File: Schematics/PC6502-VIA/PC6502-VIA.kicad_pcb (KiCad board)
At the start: 4 copper layers, 100 x 100 mm, 38 parts, among them J1 BUS, J2 Conn_02x06_Odd_Even, J3 Conn_02x06_Odd_Even, J4 Conn_02x04_Odd_Even, J5 Conn_02x04_Odd_Even, J6 Conn_02x06_Odd_Even, J7 Conn_02x06_Odd_Even, J8 Conn_02x05_Odd_Even, U1 W65C22NxP, U2 W65C22NxP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

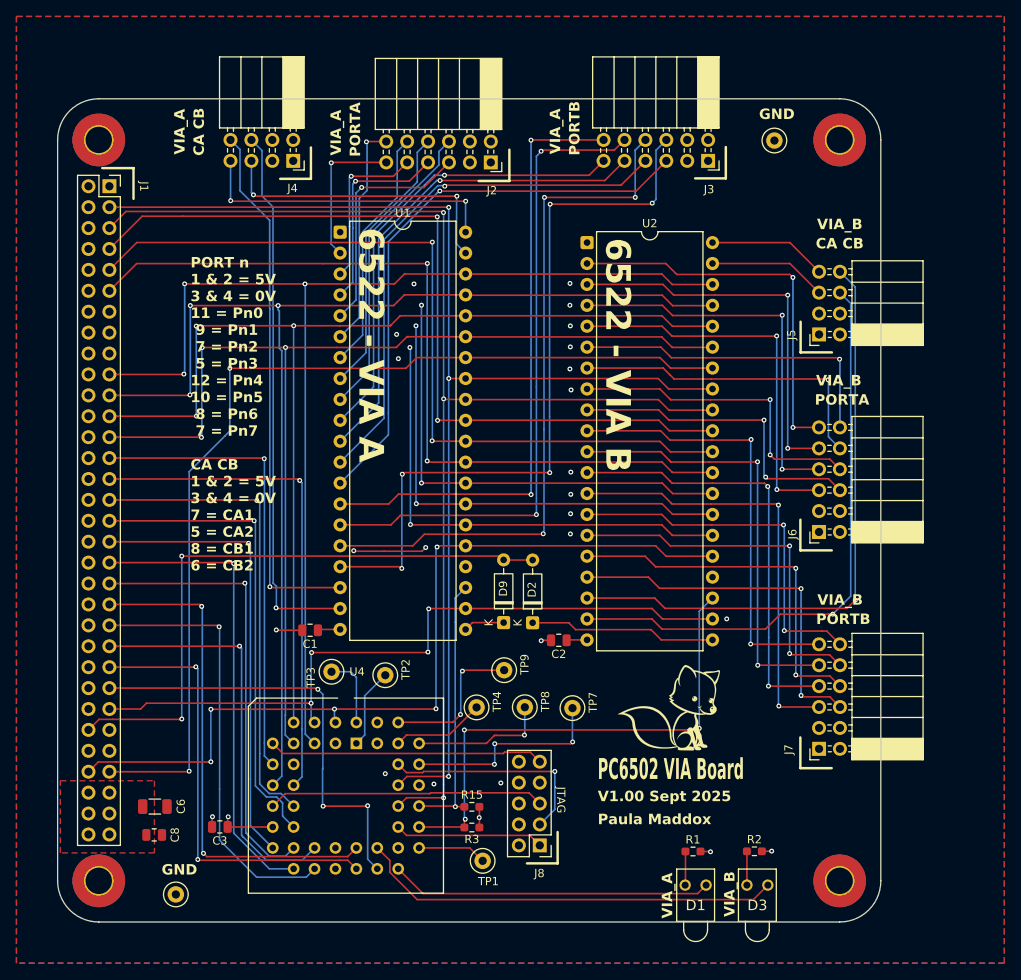
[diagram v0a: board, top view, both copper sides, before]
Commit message: V1.1 CPU, VIA and POWER PCBs uploaded
A simpler CPU board (direct link to FT245R, 74161 removed and some tidying of tracks). Fixed a couple of floating inputs to RAM/ROM
VIA is much simpler, having just the one VIA chip.
POWER board has USB-PD and a 24VDC input for higher power stuff in the future.
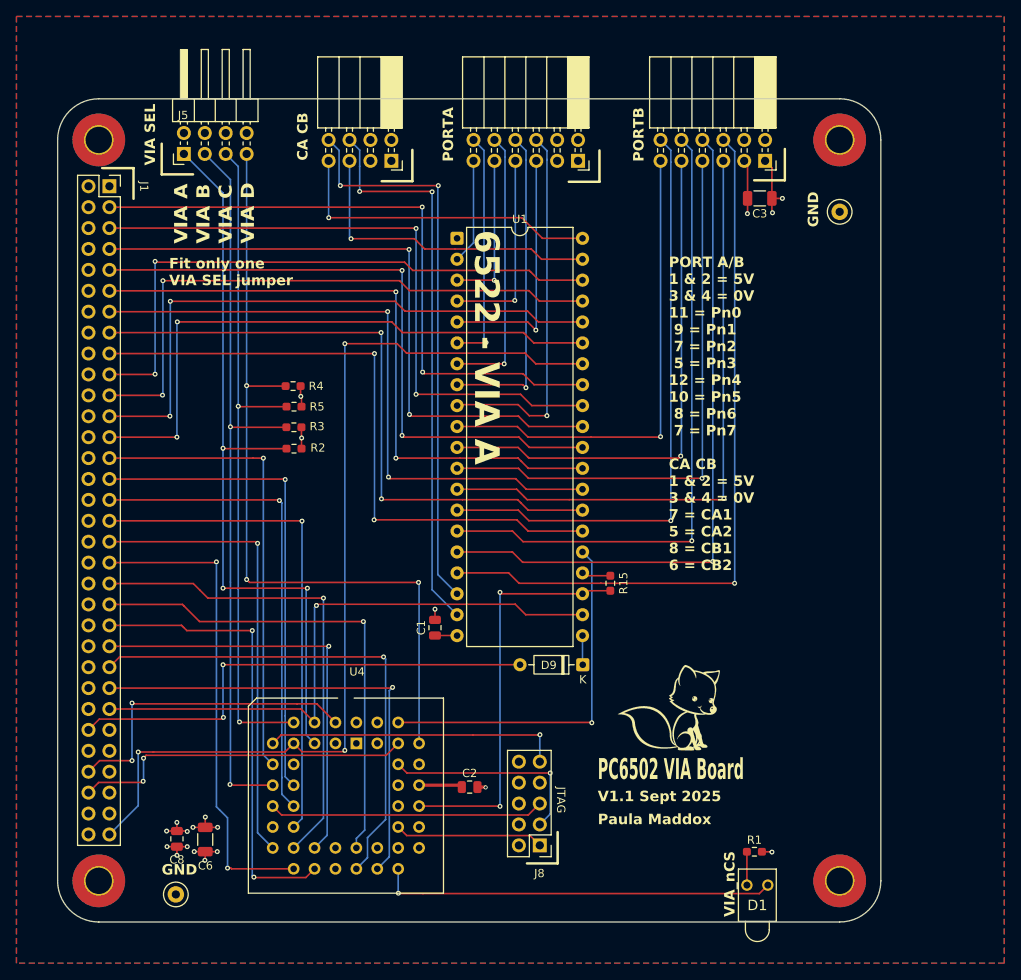
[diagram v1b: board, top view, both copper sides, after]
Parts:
- removed D2: 1N4148, Diode_THT:D_DO-35_SOD27_P7.62mm_Horizontal
- removed D3: LED, LTL-4221NHBP:LTL4221NHBP
- removed J6, J7: Conn_02x06_Odd_Even, Connector_PinSocket_2.54mm:PinSocket_2x06_P2.54mm_Horizontal
- removed TP1, TP2, TP3, TP4, TP7, TP8, TP9: TestPoint, TestPoint:TestPoint_Loop_D1.80mm_Drill1.0mm_Beaded
- removed U2: W65C22NxP, Package_DIP:DIP-40_W15.24mm
- added R4: 4K7, Resistor_SMD:R_0603_1608Metric_Pad0.98x0.95mm_HandSolder, F.Cu at (125.7, 79.9)
- added R5: 4K7, Resistor_SMD:R_0603_1608Metric_Pad0.98x0.95mm_HandSolder, F.Cu at (125.8, 82.4)
- C3: value 100nF -> 47uF; footprint Capacitor_SMD:C_0805_2012Metric -> Capacitor_SMD:C_1206_3216Metric
- J5: value Conn_02x04_Odd_Even -> VIA_SEL; footprint Connector_PinSocket_2.54mm:PinSocket_2x04_P2.54mm_Horizontal -> Connector_PinHeader_2.54mm:PinHeader_2x04_P2.54mm_Horizontal
- R2: value 470R -> 4K7
- moved C3 100.6 mm to (182.3, 57.1)
- moved J5 80.2 mm to (112.4, 51.7), turned to 90 degrees
- moved R2 74.3 mm to (125.8, 87.5), turned to 180 degrees
- moved R3 53.2 mm to (125.8, 84.9)
- moved R15 31.9 mm to (164.2, 103.8), turned to -90 degrees
- moved C2 20.9 mm to (147.1, 128.6), turned to 0 degrees
- moved C1 15.2 mm to (142.9, 109.2), turned to 90 degrees
- moved U1 14.2 mm to (145.6, 62.0)
- moved J4 11.9 mm to (137.6, 52.5)
- moved TP6 11.7 mm to (192.1, 58.7), turned to 90 degrees
- moved D9 10.9 mm to (160.8, 113.8), turned to 180 degrees
- moved J2 10.6 mm to (160.3, 52.5)
- moved D1 7.50 mm to (180.8, 140.5)
- moved R1 7.46 mm to (181.7, 136.5)
- moved C6 7.31 mm to (115.0, 135.0), turned to -90 degrees
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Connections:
- net nSLOW renamed nSLOW0
- J1 pad 12: GND -> +5V
- J1 pad 16: GND -> +5V
- J1 pad 20: GND -> +5V
- J1 pad 24: GND -> +5V
- J1 pad 28: GND -> +5V
- J1 pad 32: GND -> +5V
- J1 pad 36: GND -> +5V
- J1 pad 4: GND -> +5V
- J1 pad 40: GND -> +5V
- J1 pad 44: GND -> +5V
- J1 pad 48: GND -> +5V
- J1 pad 55: nBUSRQ -> nSLOW1
- J1 pad 57: nRES -> RDY
- J1 pad 58: CLK -> SYSCLK
- J1 pad 59: +5V -> nVP
- J1 pad 60: SPCLK -> CPU_CLK
- J1 pad 61: +5V -> nBUSRQ
- J1 pad 62: +5V -> unconnected-(J1-Pin_62-Pad62)
- J1 pad 63: +5V -> nRES
- J1 pad 64: +5V -> GND
- J1 pad 8: GND -> +5V
- J3 pad 1: unconnected-(J3-Pin_1-Pad1) -> +5V
- J4 pad 1: unconnected-(J4-Pin_1-Pad1) -> +5V
- J5 pad 1: +5V -> VIA_SEL0
- J5 pad 2: +5V -> GND
- J5 pad 3: GND -> VIA_SEL1
- J5 pad 5: /VB_CA2 -> VIA_SEL2
- J5 pad 6: /VB_CB2 -> GND
- J5 pad 7: /VB_CA1 -> VIA_SEL3
- J5 pad 8: /VB_CB1 -> GND
- R2 pad 1: Net-(D3-A) -> +5V
- R2 pad 2: +5V -> VIA_SEL0
- R3 pad 2: 6522B_CS -> VIA_SEL1
- U1 pad 25: CLK -> VIA_CLK
- U4 pad 1: Net-(U4-I/GCLR) -> unconnected-(U4-I/GCLR-Pad1)
- U4 pad 11: /A1 -> VIA_SEL1
- U4 pad 2: CLK -> SYSCLK
- U4 pad 27: Net-(D3-K) -> unconnected-(U4-I/O-Pad27)
- U4 pad 29: Net-(TP1-Pad1) -> unconnected-(U4-I/O-Pad29)
- U4 pad 31: 6522B_CS -> unconnected-(U4-I/O-Pad31)
- U4 pad 34: /D1 -> unconnected-(U4-I/O-Pad34)
- U4 pad 36: /D0 -> unconnected-(U4-I/O-Pad36)
- U4 pad 37: Net-(TP7-Pad1) -> unconnected-(U4-I/O-Pad37)
- U4 pad 39: Net-(TP8-Pad1) -> VIA_SEL3
- U4 pad 40: Net-(TP9-Pad1) -> VIA_CLK
- U4 pad 41: Net-(U4-I/O/GCLK3) -> CPU_CLK
- U4 pad 44: Net-(U4-I/OE1) -> unconnected-(U4-I/OE1-Pad44)
- U4 pad 5: /A0 -> VIA_SEL0
- U4 pad 6: /A2 -> VIA_SEL2
- U4 pad 8: /A3 -> nRES
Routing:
- net CLK: track 104.5 -> 0.00 mm, vias 5 -> 0
- net VIA_SEL3: track 0.00 -> 97.2 mm, vias 0 -> 3
- net VIA_SEL0: track 0.00 -> 92.0 mm, vias 0 -> 3
- net VIA_SEL1: track 0.00 -> 90.0 mm, vias 0 -> 2
- net VIA_SEL2: track 0.00 -> 82.2 mm, vias 0 -> 2
- net /VB_CB1: track 74.2 -> 0.00 mm, vias 1 -> 0
- net /D1: track 151.7 -> 78.2 mm, vias 3 -> 2
- net /A1: track 144.1 -> 72.4 mm, vias 3 -> 2
- net /VB_CB2: track 71.6 -> 0.00 mm, vias 1 -> 0
- net /D0: track 149.5 -> 78.1 mm, vias 3 -> 2
- net /A0: track 141.5 -> 72.1 mm, vias 3 -> 2
- net 6522B_CS: track 62.6 -> 0.00 mm, vias 3 -> 0
- net /A3: track 133.7 -> 72.5 mm, vias 3 -> 2
- net /A2: track 133.5 -> 72.4 mm, vias 3 -> 2
- net /VB_PB0: track 53.6 -> 0.00 mm, vias 2 -> 0
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- removed copper zone on F.Cu, net +5V
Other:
- board text added: "Fit only one VIA SEL jumper"
- board text added: "PORT A/B 1 & 2 = 5V 3 & 4 = 0V 11 = Pn0 9 = Pn1 7 = Pn2 5 = Pn3 12 = Pn4 10 = Pn5 8 = Pn6 7 = Pn7 CA CB 1 & 2 = 5V 3 & 4 = 0V 7 = CA1 5 = CA2 8 = CB1 6 = CB2"
- board text added: "V1.1 Sept 2025"
- board text added: "VIA A"
- board text added: "VIA B"
- board text added: "VIA C"
- board text added: "VIA D"
- board text added: "VIA SEL"
- board text added: "VIA_nCS"
- board text removed: "6522 - VIA B"
- board text removed: "PORT n 1 & 2 = 5V 3 & 4 = 0V 11 = Pn0 9 = Pn1 7 = Pn2 5 = Pn3 12 = Pn4 10 = Pn5 8 = Pn6 7 = Pn7 CA CB 1 & 2 = 5V 3 & 4 = 0V 7 = CA1 5 = CA2 8 = CB1 6 = CB2"
- board text removed: "V1.00 Sept 2025"
- board text removed: "VIA_A"
- board text removed: "VIA_B"

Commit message: Ordered Storage, FM/Speech, Dual SPI and APPLE II slot PCBs
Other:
- board text added: "PORT A/B 1 & 2 = 5V 3 & 4 = 0V 11 = Pn0 9 = Pn1 7 = Pn2 5 = Pn3 12 = Pn4 10 = Pn5 8 = Pn6 6 = Pn7 CA CB 1 & 2 = 5V 3 & 4 = 0V 7 = CA1 5 = CA2 8 = CB1 6 = CB2"
- board text removed: "PORT A/B 1 & 2 = 5V 3 & 4 = 0V 11 = Pn0 9 = Pn1 7 = Pn2 5 = Pn3 12 = Pn4 10 = Pn5 8 = Pn6 7 = Pn7 CA CB 1 & 2 = 5V 3 & 4 = 0V 7 = CA1 5 = CA2 8 = CB1 6 = CB2"
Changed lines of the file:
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@@
 		)
 	)
-	(gr_text "PORT A/B \n1 & 2 = 5V\n3 & 4 = 0V\n11 = Pn0\n 9 = Pn1\n 7 = Pn2\n 5 = Pn3\n12 = Pn4\n10 = Pn5\n 8 = Pn6\n 7 = Pn7\n\nCA CB\n1 & 2 = 5V\n3 & 4 = 0V\n7 = CA1\n5 = CA2\n8 = CB1\n6 = CB2"
+	(gr_text "PORT A/B \n1 & 2 = 5V\n3 & 4 = 0V\n11 = Pn0\n 9 = Pn1\n 7 = Pn2\n 5 = Pn3\n12 = Pn4\n10 = Pn5\n 8 = Pn6\n 6 = Pn7\n\nCA CB\n1 & 2 = 5V\n3 & 4 = 0V\n7 = CA1\n5 = CA2\n8 = CB1\n6 = CB2"
 		(at 171.3 102.4 0)
 		(layer "F.SilkS")
@@
 			(justify left bottom)
 		)
-		(render_cache "PORT A/B \n1 & 2 = 5V\n3 & 4 = 0V\n11 = Pn0\n 9 = Pn1\n 7 = Pn2\n 5 = Pn3\n12 = Pn4\n10 = Pn5\n 8 = Pn6\n 7 = Pn7\n\nCA CB\n1 & 2 = 5V\n3 & 4 = 0V\n7 = CA1\n5 = CA2\n8 = CB1\n6 = CB2"
+		(render_cache "PORT A/B \n1 & 2 = 5V\n3 & 4 = 0V\n11 = Pn0\n 9 = Pn1\n 7 = Pn2\n 5 = Pn3\n12 = Pn4\n10 = Pn5\n 8 = Pn6\n 6 = Pn7\n\nCA CB\n1 & 2 = 5V\n3 & 4 = 0V\n7 = CA1\n5 = CA2\n8 = CB1\n6 = CB2"
 			0
 			(polygon
@@
 			(polygon
 				(pts
-					(xy 173.3132 84.137508) (xy 173.171342 84.344574) (xy 173.06983 84.519378) (xy 173.001693 84.666379)
-					(xy 172.950935 84.819428) (xy 172.921252 84.968663) (xy 172.911506 85.1153) (xy 172.657306 85.1153)
-					(xy 172.663494 85.004277) (xy 172.682351 84.89052) (xy 172.714537 84.773333) (xy 172.760987 84.652033)
-					(xy 172.816399 84.53833) (xy 172.887885 84.416373) (xy 172.977319 84.28534) (xy 173.086762 84.14441)
-					(xy 172.479491 84.14441) (xy 172.479491 83.944028) (xy 173.3132 83.944028)
-				)
-			)
+					(xy 173.029466 83.937676) (xy 173.109706 83.961145) (xy 173.173072 83.997613) (xy 173.225023 84.048922)
+					(xy 173.267576 84.118259) (xy 173.300172 84.209782) (xy 173.070245 84.241809) (xy 173.047386 84.187164)
+					(xy 173.015975 84.151037) (xy 172.975446 84.129437) (xy 172.92275 84.121766) (xy 172.87612 84.1276)
+					(xy 172.835747 84.144583) (xy 172.800068 84.173198) (xy 172.768354 84.21552) (xy 172.739703 84.280675)
+					(xy 172.720198 84.370042) (xy 172.71283 84.490425) (xy 172.742186 84.450457) (xy 172.778088 84.417384)
+					(xy 172.821241 84.390699) (xy 172.894023 84.364906) (xy 172.978274 84.355958) (xy 173.057203 84.362752)
+					(xy 173.125211 84.382153) (xy 173.184313 84.413484) (xy 173.235963 84.457157) (xy 173.277371 84.510396)
+					(xy 173.307535 84.572453) (xy 173.32645 84.645028) (xy 173.333129 84.730356) (xy 173.325553 84.823697)
+					(xy 173.304127 84.902638) (xy 173.269953 84.969778) (xy 173.222935 85.027051) (xy 173.164849 85.073059)
+					(xy 173.096723 85.106612) (xy 173.016599 85.127692) (xy 172.921897 85.135152) (xy 172.838125 85.128356)
+					(xy 172.764828 85.10886) (xy 172.700167 85.077308) (xy 172.64276 85.033407) (xy 172.591779 84.975947)
+					(xy 172.543124 84.894564) (xy 172.50639 84.796191) (xy 172.489432 84.711202) (xy 172.730201 84.711202)
+					(xy 172.736216 84.775038) (xy 172.753421 84.829838) (xy 172.781382 84.877385) (xy 172.819504 84.915496)
+					(xy 172.863085 84.937615) (xy 172.914142 84.945161) (xy 172.965321 84.938666) (xy 173.007072 84.920177)
+					(xy 173.04163 84.88956) (xy 173.066721 84.849933) (xy 173.082691 84.800108) (xy 173.088468 84.737335)
+					(xy 173.082534 84.675853) (xy 173.06614 84.627376) (xy 173.040312 84.589065) (xy 173.005031 84.559829)
+					(xy 172.961734 84.541912) (xy 172.908016 84.535557) (xy 172.857917 84.541205) (xy 172.815864 84.557345)
+					(xy 172.780064 84.583869) (xy 172.752732 84.618807) (xy 172.736064 84.660584) (xy 172.730201 84.711202)
+					(xy 172.489432 84.711202) (xy 172.48272 84.67756) (xy 172.474218 84.534782) (xy 172.480023 84.406069)
+					(xy 172.496119 84.299051) (xy 172.520835 84.210571) (xy 172.552954 84.137823) (xy 172.591779 84.078417)
+					(xy 172.642147 84.025284) (xy 172.69971 83.984185) (xy 172.765455 83.954309) (xy 172.84089 83.935674)
+					(xy 172.927946 83.929139)
+				)
+			)
